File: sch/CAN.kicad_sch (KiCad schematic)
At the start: 18 parts, among them U2 TJA1051T/3, U3 TJA1051T/3

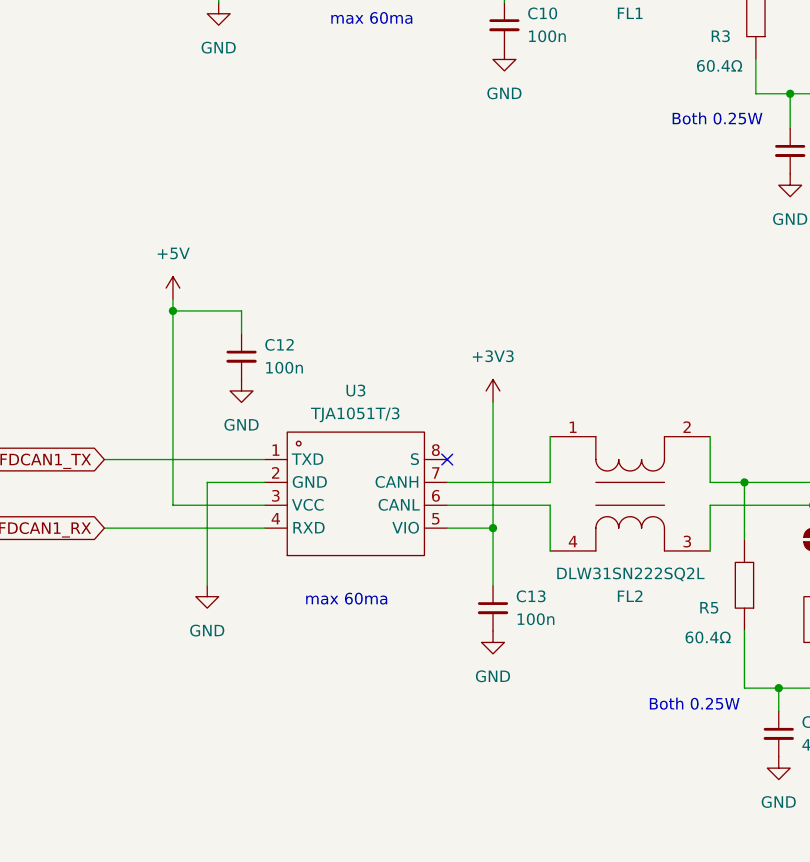
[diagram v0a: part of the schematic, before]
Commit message: change 2x22u to 3x10u plot all order jlcpcb + lcsc
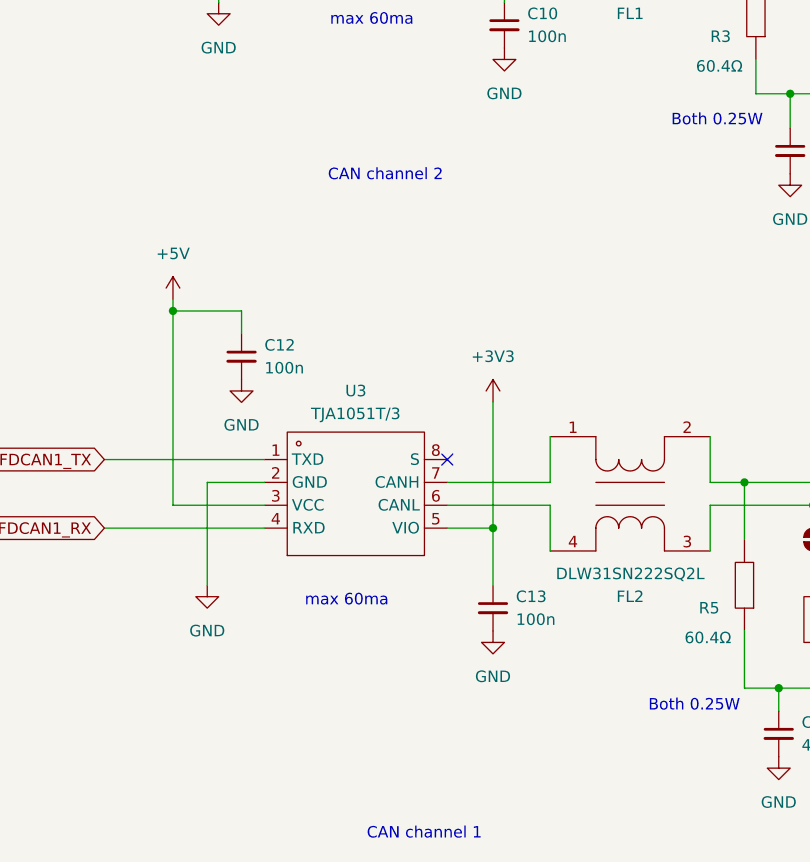
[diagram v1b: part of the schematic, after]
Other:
- note added: "CAN channel 1"
- note added: "CAN channel 2"
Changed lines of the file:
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@@
+		)
+	)
+	(text "CAN channel 2"
+		(exclude_from_sim no)
+		(at 131.572 72.644 0)
+		(effects
+			(font
+				(size 1.27 1.27)
+			)
 		)
 	)
@@
 		(effects
 			(font
+				(size 1.27 1.27)
+			)
+		)
+	)
+	(text "CAN channel 1"
+		(exclude_from_sim no)
+		(at 135.89 145.796 0)
+		(effects
+			(font
